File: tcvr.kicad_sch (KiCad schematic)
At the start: 34 parts, among them J1 9V, J2 anterna 50 Ohm, Q1 BC817 86-05-47, Q2 2N7002, Q3 PZT2222A 86-02-43, SW1 SW_DPST_x2, U1 LM386 89-24-08, Y1 3579kHz 40-00-62

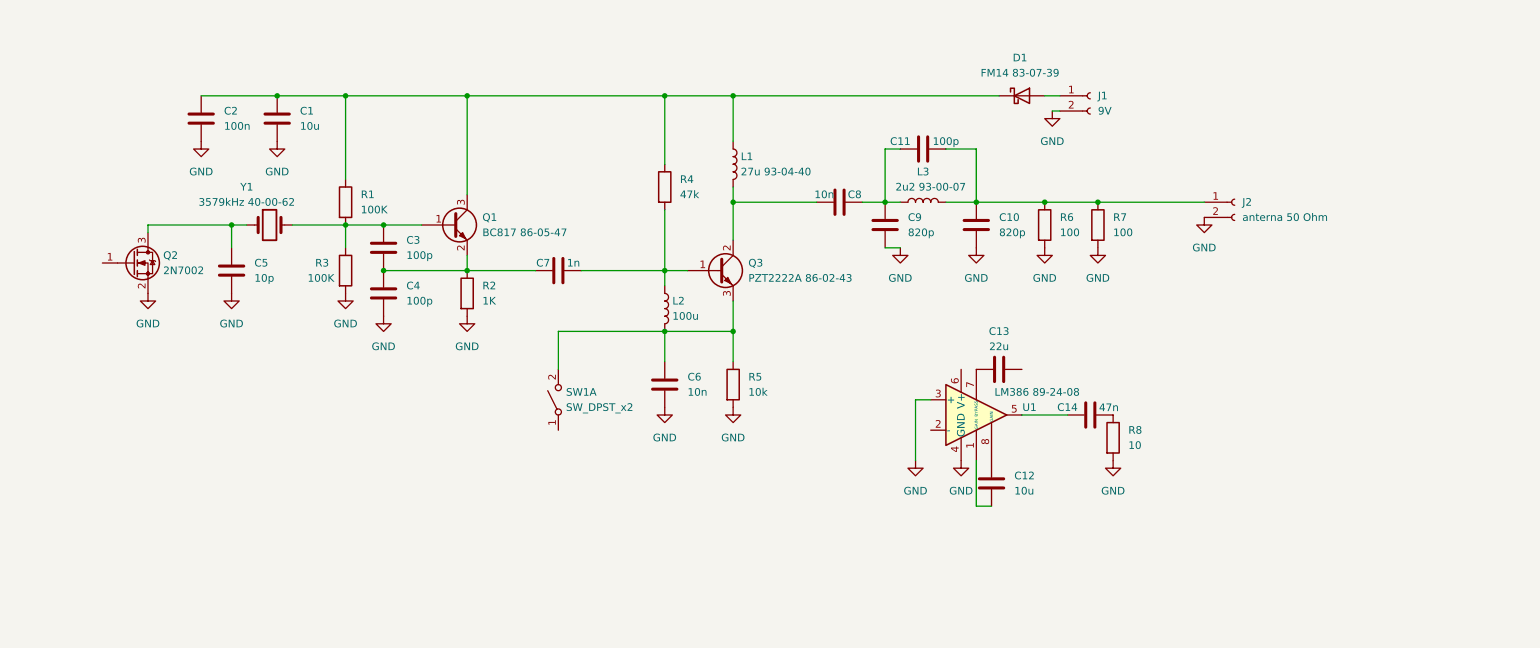
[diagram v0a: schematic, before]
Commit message: changed schematic
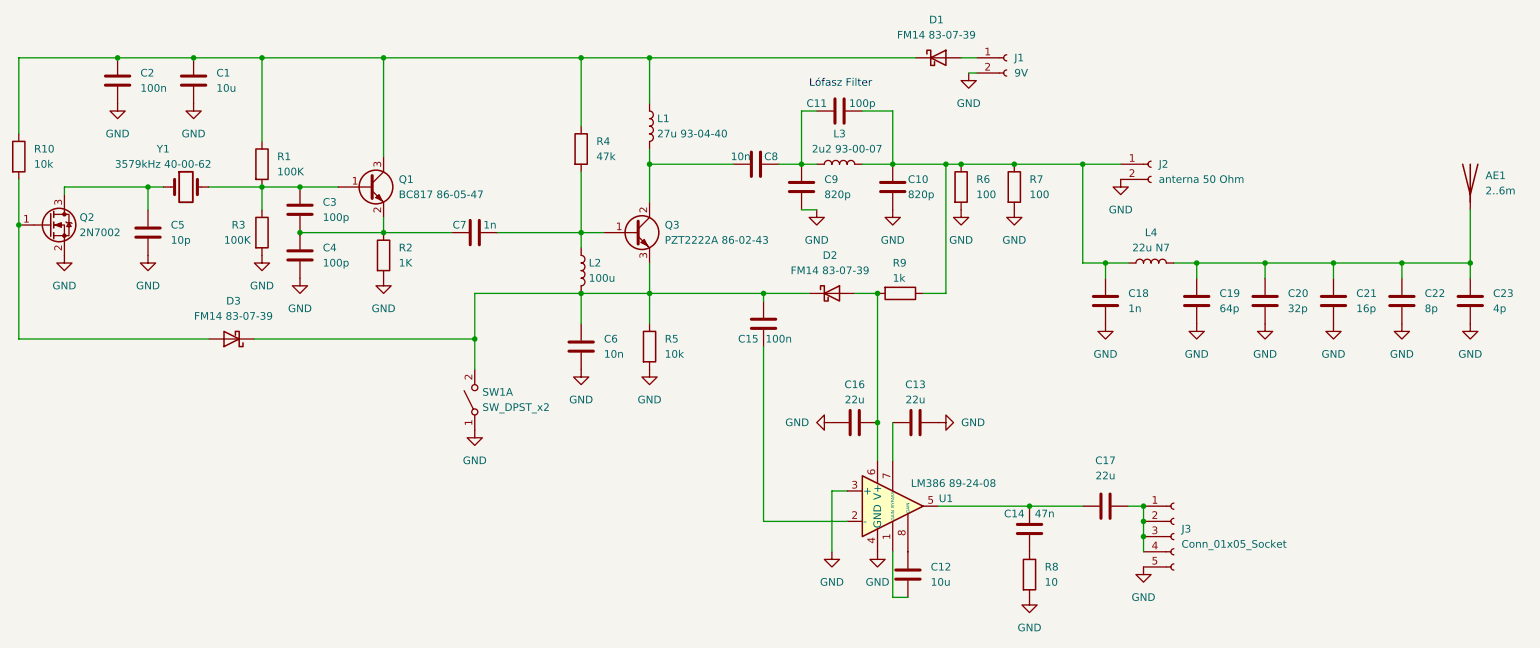
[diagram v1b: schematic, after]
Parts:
- added AE1: 2..6m, symbol Device:Antenna
- added C15: 100n, symbol Device:C
- added C16, C17: 22u, symbol Device:C
- added C18: 1n, symbol Device:C
- added C19: 64p, symbol Device:C
- added C20: 32p, symbol Device:C
- added C21: 16p, symbol Device:C
- added C22: 8p, symbol Device:C
- added C23: 4p, symbol Device:C
- added D2, D3: FM14 83-07-39, symbol Device:D_Schottky
- added J3: Conn_01x05_Socket, symbol Connector:Conn_01x05_Socket
- added L4: 22u N7, symbol Device:L
- added R10: 10k, symbol Device:R
- added R9: 1k, symbol Device:R
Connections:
- net GND: now also C13.2, SW1.1 (A), C16.2, C18.2, C19.2, C20.2, C21.2, C22.2, C23.2, J3.5 (Pin_5)
- net at C1.1, C2.1, D1.1 (K)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: now also R10.1
- net at C10.1, C11.2, J2.1 (Pin_1)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: now also C18.1, L4.1, R9.1
- net at C14.1: now also U1.5, C17.1; no longer R8.1
- net at C14.2: now also R8.1; no longer U1.5
- net at C6.1, L2.2, Q3.3 (E)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: now also C15.2, D2.1 (K), D3.1 (K)
- net at U1.2 (-): now also C15.1
- net at U1.6 (V+): now also C16.1, D2.2 (A), R9.2
- net at Q2.1 (G): now also D3.2 (A), R10.2
- new net: AE1.1 (A), C19.1, C20.1, C21.1, C22.1, C23.1, L4.2
- new net: C17.2, J3.1 (Pin_1), J3.2 (Pin_2), J3.3 (Pin_3), J3.4 (Pin_4)
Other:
- note added: "Lófasz Filter"
- moved on the sheet: C1, C10, C11, C12, C13, C14, C2, C3, C4, C5, C6, C7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

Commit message: Modified sch
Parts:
- AE1: footprint (none) -> tcvr:key
- C1, D1, D2, D3: footprint (none) -> Capacitor_SMD:C_1206_3216Metric
- C10, C11, C12, C15, C16, C17, C18, C19, C2, C20, C21, C22, C23, C3, C4, C5, C6, C7, C8, C9: footprint (none) -> Capacitor_SMD:C_0805_2012Metric
- C13: renamed from C14; footprint (none) -> Capacitor_SMD:C_0805_2012Metric
- C14: renamed from C13; footprint (none) -> Capacitor_SMD:C_0805_2012Metric
- J1: value 9V -> 9V 43-04-70; footprint (none) -> Connector_PinHeader_2.54mm:PinHeader_1x02_P2.54mm_Vertical
- J2: footprint (none) -> tcvr:coax
- J3: value Conn_01x05_Socket -> jack 43-08-39
- L1: value 27u 93-04-40 -> 55-00-84 33uH 4r
- L2: value 100u -> 100u 93-04-44 1210
- L3: value 2u2 93-00-07 -> 2u2 55-02-11
- L4: value 22u N7 -> 22u N7 55-00-66
- R1, R10, R2, R3, R4, R5, R6, R7, R8, R9: footprint (none) -> Resistor_SMD:R_0805_2012Metric
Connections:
- net at C1.1, C2.1, D1.1 (K)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: now also R9.1
- net at C10.1, C11.2, C18.1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: no longer R9.1
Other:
- moved on the sheet: AE1, D1, J1, R6, R7

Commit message: made footprint assign
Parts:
- AE1: footprint tcvr:key -> Inductor_THT:L_Axial_L9.5mm_D4.0mm_P12.70mm_Horizontal_Fastron_SMCC
- C12, C14, C17: footprint Capacitor_SMD:C_0805_2012Metric -> Capacitor_SMD:C_1206_3216Metric
- D1, D2, D3: footprint Capacitor_SMD:C_1206_3216Metric -> Diode_SMD:D_SOD-323_HandSoldering
- J3: footprint (none) -> tcvr:jack
- L1, L2: footprint (none) -> Inductor_SMD:L_1210_3225Metric
- L3, L4: footprint (none) -> Inductor_THT:L_Axial_L9.5mm_D4.0mm_P12.70mm_Horizontal_Fastron_SMCC
- SW1: footprint (none) -> tcvr:key
- U1: footprint (none) -> Package_SO:HSOP-8-1EP_3.9x4.9mm_P1.27mm_EP2.41x3.1mm_ThermalVias
- Y1: footprint (none) -> Crystal:Crystal_HC49-U_Horizontal
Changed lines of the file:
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@@
       (effects (font (size 1.27 1.27)))
     )
-    (property "Footprint" "" (at 156.21 49.53 0)
+    (property "Footprint" "Inductor_THT:L_Axial_L9.5mm_D4.0mm_P12.70mm_Horizontal_Fastron_SMCC" (at 156.21 49.53 0)
       (effects (font (size 1.27 1.27)) hide)
     )
@@
       (effects (font (size 1.27 1.27)))
     )
-    (property "Footprint" "Capacitor_SMD:C_0805_2012Metric" (at 204.47 105.7148 0)
+    (property "Footprint" "Capacitor_SMD:C_1206_3216Metric" (at 204.47 105.7148 0)
       (effects (font (size 1.27 1.27)) hide)
     )
@@
       (effects (font (size 1.27 1.27)))
     )
-    (property "Footprint" "" (at 208.28 66.04 0)
+    (property "Footprint" "Inductor_THT:L_Axial_L9.5mm_D4.0mm_P12.70mm_Horizontal_Fastron_SMCC" (at 208.28 66.04 0)
       (effects (font (size 1.27 1.27)) hide)
     )
@@
       (effects (font (size 1.27 1.27)) (justify left))
     )
-    (property "Footprint" "" (at 212.09 111.76 0)
+    (property "Footprint" "tcvr:jack" (at 212.09 111.76 0)
       (effects (font (size 1.27 1.27)) hide)
     )
@@
       (effects (font (size 1.27 1.27)))
     )
-    (property "Footprint" "Capacitor_SMD:C_1206_3216Metric" (at 204.47 31.75 0)
+    (property "Footprint" "Diode_SMD:D_SOD-323_HandSoldering" (at 204.47 31.75 0)
       (effects (font (size 1.27 1.27)) hide)
     )
@@
       (effects (font (size 1.27 1.27)) (justify right))
     )
-    (property "Footprint" "" (at 95.25 88.9 0)
+    (property "Footprint" "tcvr:key" (at 95.25 88.9 0)
       (effects (font (size 1.27 1.27)) hide)
     )
@@
       (effects (font (size 1.27 1.27)) (justify left))
     )
-    (property "Footprint" "" (at 113.03 67.31 0)
+    (property "Footprint" "Inductor_SMD:L_1210_3225Metric" (at 113.03 67.31 0)
       (effects (font (size 1.27 1.27)) hide)
     )
@@
       (effects (font (size 1.27 1.27)) (justify left))
     )
-    (property "Footprint" "" (at 124.46 43.18 0)
+    (property "Footprint" "Inductor_SMD:L_1210_3225Metric" (at 124.46 43.18 0)
       (effects (font (size 1.27 1.27)) hide)
     )
@@
       (effects (font (size 1.27 1.27)) (justify left))
     )
-    (property "Footprint" "tcvr:key" (at 261.62 58.42 0)
+    (property "Footprint" "Inductor_THT:L_Axial_L9.5mm_D4.0mm_P12.70mm_Horizontal_Fastron_SMCC" (at 261.62 58.42 0)
       (effects (font (size 1.27 1.27)) hide)
     )
@@
       (effects (font (size 1.27 1.27)) (justify left))
     )
-    (property "Footprint" "Capacitor_SMD:C_0805_2012Metric" (at 168.6052 121.92 0)
+    (property "Footprint" "Capacitor_SMD:C_1206_3216Metric" (at 168.6052 121.92 0)
       (effects (font (size 1.27 1.27)) hide)
     )
@@
       (effects (font (size 1.27 1.27)))
     )
-    (property "Footprint" "Capacitor_SMD:C_0805_2012Metric" (at 172.72 91.7448 0)
+    (property "Footprint" "Capacitor_SMD:C_1206_3216Metric" (at 172.72 91.7448 0)
       (effects (font (size 1.27 1.27)) hide)
     )
@@
       (effects (font (size 1.27 1.27)))
     )
-    (property "Footprint" "Capacitor_SMD:C_1206_3216Metric" (at 54.61 78.74 0)
+    (property "Footprint" "Diode_SMD:D_SOD-323_HandSoldering" (at 54.61 78.74 0)
       (effects (font (size 1.27 1.27)) hide)
     )
@@
       (effects (font (size 1.27 1.27)))
     )
-    (property "Footprint" "" (at 167.64 104.14 0)
+    (property "Footprint" "Package_SO:HSOP-8-1EP_3.9x4.9mm_P1.27mm_EP2.41x3.1mm_ThermalVias" (at 167.64 104.14 0)
       (effects (font (size 1.27 1.27)) hide)
     )
@@
       (effects (font (size 1.27 1.27)))
     )
-    (property "Footprint" "" (at 46.99 53.34 0)
+    (property "Footprint" "Crystal:Crystal_HC49-U_Horizontal" (at 46.99 53.34 0)
       (effects (font (size 1.27 1.27)) hide)
     )
@@
       (effects (font (size 1.27 1.27)))
     )
-    (property "Footprint" "Capacitor_SMD:C_1206_3216Metric" (at 154.94 71.12 0)
-      (effects (font (size 1.27 1.27)) hide)
-    )
+    (property "Footprint" "Diode_SMD:D_SOD-323_HandSoldering" (at 154.94 71.12 0)
+      (effects (font (size 1.27 1.27)) hide)
+    )

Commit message: modified netlist
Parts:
- C16: footprint Capacitor_SMD:C_0805_2012Metric -> Capacitor_SMD:C_1206_3216Metric
- L1: footprint Inductor_SMD:L_1210_3225Metric -> Inductor_THT:L_Axial_L9.5mm_D4.0mm_P12.70mm_Horizontal_Fastron_SMCC
- U1: footprint Package_SO:HSOP-8-1EP_3.9x4.9mm_P1.27mm_EP2.41x3.1mm_ThermalVias -> Package_SO:SOIC-8_3.9x4.9mm_P1.27mm
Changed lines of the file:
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@@
       (effects (font (size 1.27 1.27)) (justify left))
     )
-    (property "Footprint" "Inductor_SMD:L_1210_3225Metric" (at 124.46 43.18 0)
+    (property "Footprint" "Inductor_THT:L_Axial_L9.5mm_D4.0mm_P12.70mm_Horizontal_Fastron_SMCC" (at 124.46 43.18 0)
       (effects (font (size 1.27 1.27)) hide)
     )
@@
       (effects (font (size 1.27 1.27)))
     )
-    (property "Footprint" "Capacitor_SMD:C_0805_2012Metric" (at 154.94 93.6752 0)
+    (property "Footprint" "Capacitor_SMD:C_1206_3216Metric" (at 154.94 93.6752 0)
       (effects (font (size 1.27 1.27)) hide)
     )
@@
       (effects (font (size 1.27 1.27)))
     )
-    (property "Footprint" "Package_SO:HSOP-8-1EP_3.9x4.9mm_P1.27mm_EP2.41x3.1mm_ThermalVias" (at 167.64 104.14 0)
-      (effects (font (size 1.27 1.27)) hide)
-    )
+    (property "Footprint" "Package_SO:SOIC-8_3.9x4.9mm_P1.27mm" (at 167.64 104.14 0)
+      (effects (font (size 1.27 1.27)) hide)
+    )

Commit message: updated netlist
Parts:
- AE1: footprint Inductor_THT:L_Axial_L9.5mm_D4.0mm_P12.70mm_Horizontal_Fastron_SMCC -> Connector_PinHeader_2.54mm:PinHeader_1x01_P2.54mm_Vertical
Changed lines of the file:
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@@
       (effects (font (size 1.27 1.27)) (justify left))
     )
-    (property "Footprint" "Inductor_THT:L_Axial_L9.5mm_D4.0mm_P12.70mm_Horizontal_Fastron_SMCC" (at 261.62 58.42 0)
+    (property "Footprint" "Connector_PinHeader_2.54mm:PinHeader_1x01_P2.54mm_Vertical" (at 261.62 58.42 0)
       (effects (font (size 1.27 1.27)) hide)
     )

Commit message: hole added
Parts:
- added J4: hole, tcvr:hole, symbol Connector:Conn_01x01_Pin
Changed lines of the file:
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@@
+    )
+  )
+  (symbol (lib_id "Connector:Conn_01x01_Pin") (at 119.38 114.3 0) (unit 1)
+    (in_bom yes) (on_board yes) (dnp no) (fields_autoplaced)
+    (property "Reference" "J4" (at 120.015 109.22 0)
+      (effects (font (size 1.27 1.27)))
+    )
+    (property "Value" "hole" (at 120.015 111.76 0)
+      (effects (font (size 1.27 1.27)))
+    )
+    (property "Footprint" "tcvr:hole" (at 119.38 114.3 0)
+      (effects (font (size 1.27 1.27)) hide)
+    )
+    (property "Datasheet" "~" (at 119.38 114.3 0)
+      (effects (font (size 1.27 1.27)) hide)
+    )
+    (pin "1")
+    (instances
+      (project "tcvr"
+        (path "/e38ed3ed-b352-46bb-ab47-506942b26e19"
+          (reference "J4") (unit 1)
+        )
+      )
     )
   )

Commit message: updated pcb
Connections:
- net GND: now also J4.1 (Pin_1)
